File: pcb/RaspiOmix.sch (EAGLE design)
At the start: 48 parts, among them IC1 MCP3424-E/SL, IC2 DS1307

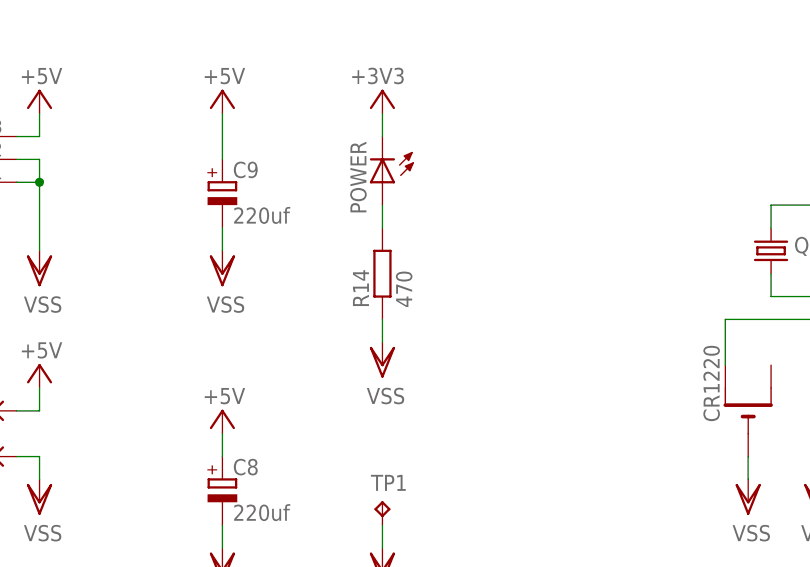
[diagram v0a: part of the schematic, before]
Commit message: Move C9 label
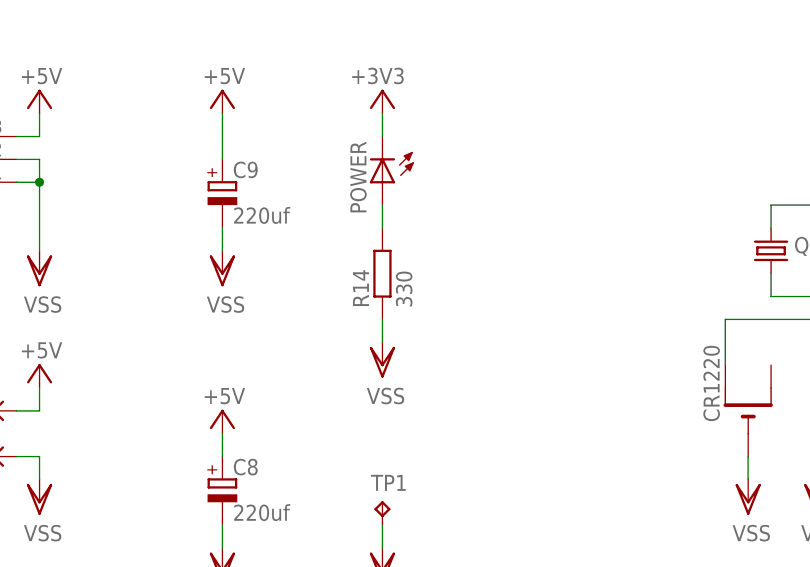
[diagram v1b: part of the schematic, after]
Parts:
- R14: value 470 -> 330
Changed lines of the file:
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@@
 <part name="VSS41" library="supply1" deviceset="VSS" device=""/>
 <part name="POWER" library="led" deviceset="LED" device="CHIPLED_0805"/>
-<part name="R14" library="rcl" deviceset="R-EU_" device="M0805" value="470"/>
+<part name="R14" library="rcl" deviceset="R-EU_" device="M0805" value="330"/>
 <part name="VSS32" library="supply1" deviceset="VSS" device=""/>
 <part name="P+12" library="supply1" deviceset="+5V" device=""/>

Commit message: PCB
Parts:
- added JP1: (no value), jumper:JP1E
- added SJ1: (no value), jumper:SJ
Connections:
- net IO0: now also CON_IO_3.2
- net IO1: now also CON_IO_0.2
- net IO2: now also CON_IO_1.2
- net IO3: now also CON_IO_2.2
- net N$1: now also CON_AN_3.2
- net N$2: now also CON_AN_0.2
- net N$3: now also CON_AN_1.2
- net N$58: now also JP1.1, SJ1.2
- net N$8: now also CON_AN_2.2
- net PI_DIP0: now also U$3.7-GPIO7; no longer U$3.12-GPIO1
- net PI_IO0: now also U$3.12-GPIO1; no longer U$3.7-GPIO7
- net VSS: now also JP1.2, SJ1.1
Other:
- moved on the sheet: CON_AN_0, CON_AN_1, CON_AN_2, CON_AN_3, CR1220

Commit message: PCB 1.1.1
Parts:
- added IO6: TPPAD1-13, testpad:TPPAD1-13
- R20, R22, R24, R26: value 10k -> 10k 1%
- R21, R23, R25, R27: value 6.8k -> 6.8k 1%
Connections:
- net N$1 renamed AN0
- net N$2 renamed AN1
- net N$3 renamed AN2
- net N$8 renamed AN3
- new net PI_IO6: IO6.TP, U$3.22-GPIO6
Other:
- note added: "IO"
- moved on the sheet: R1, R2, SW1

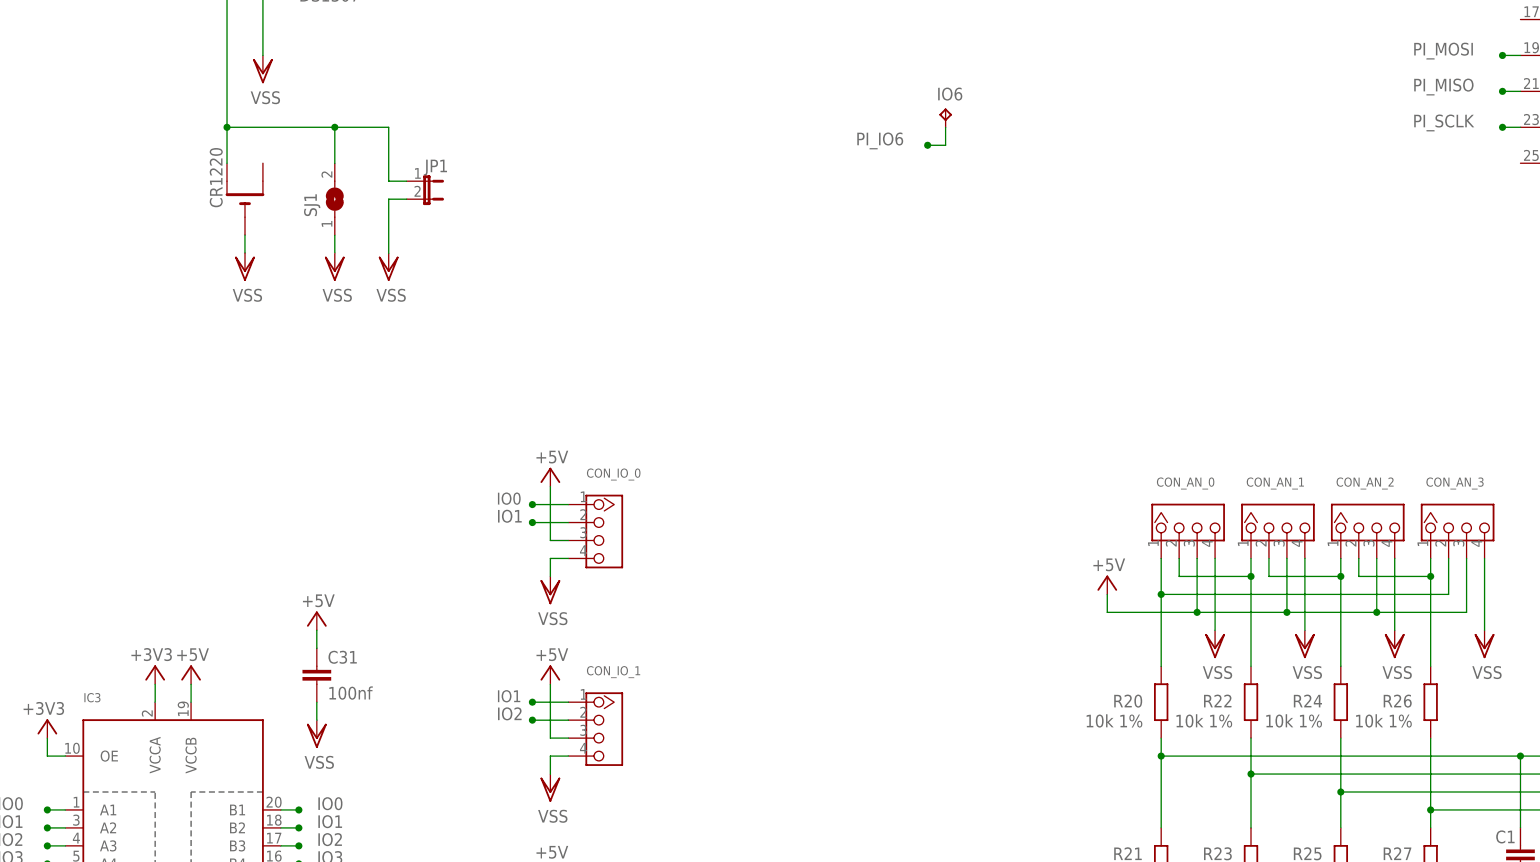
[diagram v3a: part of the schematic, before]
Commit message: New RaspiO'Mix+ hat
Schema + PCB in progress…
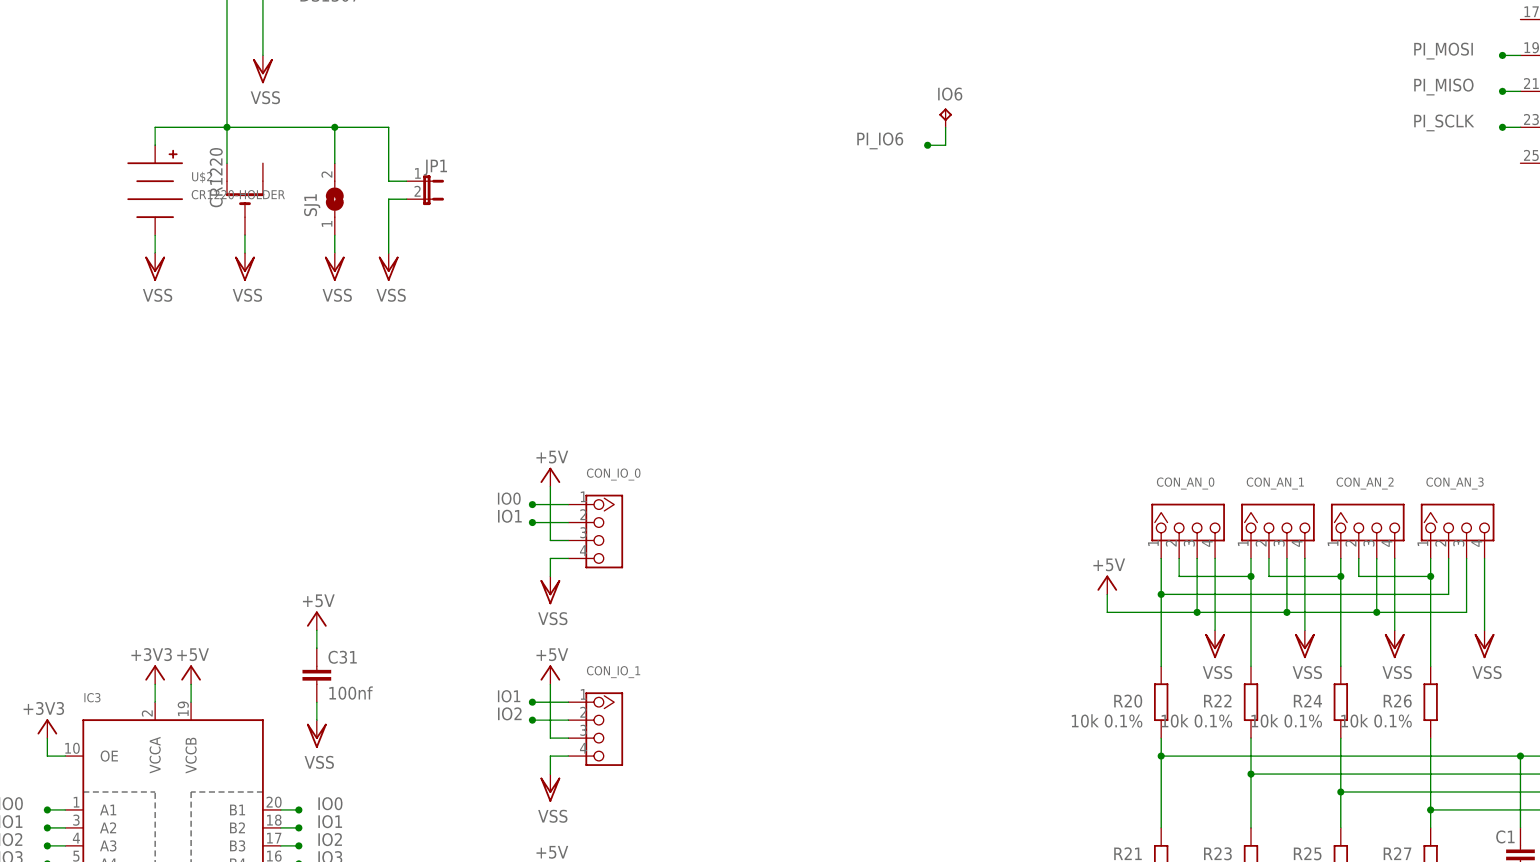
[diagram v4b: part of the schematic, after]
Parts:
- added U$2: CR1220-HOLDER, battery-holder:CR1220-HOLDER
- R20, R22, R24, R26: value 10k 1% -> 10k 0.1%
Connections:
- net N$58: now also U$2.POS
- net VSS: now also U$2.NEG
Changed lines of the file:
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@@
 <part name="VSS6" library="supply1" deviceset="VSS" device=""/>
 <part name="+3V5" library="supply1" deviceset="+3V3" device=""/>
-<part name="R26" library="rcl" deviceset="R-EU_" device="M0805" value="10k 1%"/>
-<part name="R24" library="rcl" deviceset="R-EU_" device="M0805" value="10k 1%"/>
-<part name="R22" library="rcl" deviceset="R-EU_" device="M0805" value="10k 1%"/>
-<part name="R20" library="rcl" deviceset="R-EU_" device="M0805" value="10k 1%"/>
+<part name="R26" library="rcl" deviceset="R-EU_" device="M0805" value="10k 0.1%"/>
+<part name="R24" library="rcl" deviceset="R-EU_" device="M0805" value="10k 0.1%"/>
+<part name="R22" library="rcl" deviceset="R-EU_" device="M0805" value="10k 0.1%"/>
+<part name="R20" library="rcl" deviceset="R-EU_" device="M0805" value="10k 0.1%"/>
 <part name="R27" library="rcl" deviceset="R-EU_" device="M0805" value="6.8k 1%"/>
 <part name="R25" library="rcl" deviceset="R-EU_" device="M0805" value="6.8k 1%"/>
@@
 <part name="VSS36" library="supply1" deviceset="VSS" device=""/>
 <part name="IO6" library="testpad" deviceset="TP" device="PAD1-13"/>
+<part name="U$2" library="battery-holder" deviceset="CR1220-HOLDER" device=""/>
+<part name="VSS37" library="supply1" deviceset="VSS" device=""/>
 </parts>
 <sheets>
@@
 </instance>
 <instance part="IO6" gate="G$1" x="218.44" y="170.18"/>
+<instance part="U$2" gate="G$1" x="106.68" y="157.48"/>
+<instance part="VSS37" gate="G$1" x="106.68" y="147.32" smashed="yes">
+<attribute name="VALUE" x="109.22" y="144.78" size="1.778" layer="96" rot="R180"/>
+</instance>
 </instances>
 <busses>
@@
 <wire x1="139.7" y1="157.48" x2="139.7" y2="149.86" width="0.1524" layer="91"/>
 <pinref part="VSS36" gate="G$1" pin="VSS"/>
+</segment>
+<segment>
+<pinref part="U$2" gate="G$1" pin="NEG"/>
+<wire x1="106.68" y1="152.4" x2="106.68" y2="149.86" width="0.1524" layer="91"/>
+<pinref part="VSS37" gate="G$1" pin="VSS"/>
 </segment>
 </net>
@@
 <junction x="132.08" y="167.64"/>
 <junction x="116.84" y="167.64"/>
-</segment>
-</net>
+<wire x1="116.84" y1="167.64" x2="106.68" y2="167.64" width="0.1524" layer="91"/>
+<pinref part="U$2" gate="G$1" pin="POS"/>
+<wire x1="106.68" y1="167.64" x2="106.68" y2="165.1" width="0.1524" layer="91"/>
+</segment>
+</net>
